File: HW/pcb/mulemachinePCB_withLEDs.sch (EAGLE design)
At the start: 29 parts, among them IC1 LD117AV50, IC2 MEGA8-P, J1 DCJ0202, Q1 16Mhz

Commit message: finished layout for PCB. implemented trace widths for PWR and GND. Lined up hole placement to match with Front panel laser design.
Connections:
- net N$7 renamed P1
- net N$8 renamed P2
- net N$9 renamed P3
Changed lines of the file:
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@@
 <clearance class="0" value="0.254"/>
 </class>
-<class number="1" name="Power" width="0.508" drill="0.508">
+<class number="1" name="Power" width="0.7874" drill="0.508">
 <clearance class="1" value="0.254"/>
 </class>
@@
 </segment>
 </net>
-<net name="N$7" class="0">
+<net name="P1" class="1">
 <segment>
 <pinref part="T1" gate="G$1" pin="C"/>
@@
 <pinref part="D1" gate="1" pin="A"/>
 <wire x1="165.1" y1="104.14" x2="157.48" y2="104.14" width="0.1524" layer="91"/>
-</segment>
-</net>
-<net name="N$8" class="0">
+<label x="147.32" y="99.06" size="1.778" layer="95"/>
+</segment>
+</net>
+<net name="P2" class="1">
 <segment>
 <pinref part="X2" gate="G$1" pin="5"/>
@@
 <pinref part="D2" gate="1" pin="A"/>
 <wire x1="165.1" y1="96.52" x2="157.48" y2="96.52" width="0.1524" layer="91"/>
-</segment>
-</net>
-<net name="N$9" class="0">
+<label x="162.56" y="91.44" size="1.778" layer="95"/>
+</segment>
+</net>
+<net name="P3" class="1">
 <segment>
 <pinref part="X2" gate="G$1" pin="9"/>
@@
 <wire x1="195.58" y1="86.36" x2="195.58" y2="93.98" width="0.1524" layer="91"/>
 <junction x="195.58" y="93.98"/>
-</segment>
-</net>
+<label x="203.2" y="91.44" size="1.778" layer="95"/>
+</segment>
+</net>

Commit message: ordered MM v1.0 of PCB. Gerber files contained in HW/pcb/mulemachinePCB_withLEDs_2022-02-17.zip
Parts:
- C5: value (none) -> 470uF
- R7: value 200 -> 10k
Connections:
- removed net SWTPOT: IC2.PC4(ADC4/SDA), R11.S
- new net SOURRPOT: IC2.PC5(ADC5/SCL), R10.S
- net STRPOT: now also IC2.PC4(ADC4/SDA), R11.S; no longer IC2.PC5(ADC5/SCL), R10.S
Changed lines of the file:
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@@
 <part name="C2" library="capacitor-wima" library_urn="urn:adsk.eagle:library:116" deviceset="C" device="2,5-3" package3d_urn="urn:adsk.eagle:package:5436/1" value="22pF"/>
 <part name="C3" library="capacitor-wima" library_urn="urn:adsk.eagle:library:116" deviceset="C" device="2,5-3" package3d_urn="urn:adsk.eagle:package:5436/1" value="22pF"/>
-<part name="R7" library="rcl" library_urn="urn:adsk.eagle:library:334" deviceset="R-US_" device="0207/10" package3d_urn="urn:adsk.eagle:package:23491/2" value="200"/>
+<part name="R7" library="rcl" library_urn="urn:adsk.eagle:library:334" deviceset="R-US_" device="0207/10" package3d_urn="urn:adsk.eagle:package:23491/2" value="10k"/>
 <part name="SUPPLY1" library="supply2" library_urn="urn:adsk.eagle:library:372" deviceset="GND" device=""/>
 <part name="LED1" library="led" library_urn="urn:adsk.eagle:library:259" deviceset="LED" device="5MM" package3d_urn="urn:adsk.eagle:package:15799/2"/>
@@
 <part name="R10" library="pot" library_urn="urn:adsk.eagle:library:331" deviceset="US-EVU" device="L" package3d_urn="urn:adsk.eagle:package:22736/1" technology="F3"/>
 <part name="R11" library="pot" library_urn="urn:adsk.eagle:library:331" deviceset="US-EVU" device="L" package3d_urn="urn:adsk.eagle:package:22736/1" technology="F3"/>
-<part name="C5" library="rcl" library_urn="urn:adsk.eagle:library:334" deviceset="CPOL-US" device="153CLV-0605" package3d_urn="urn:adsk.eagle:package:23398/2"/>
+<part name="C5" library="rcl" library_urn="urn:adsk.eagle:library:334" deviceset="CPOL-US" device="153CLV-0605" package3d_urn="urn:adsk.eagle:package:23398/2" value="470uF"/>
 <part name="SUPPLY11" library="supply2" library_urn="urn:adsk.eagle:library:372" deviceset="GND" device=""/>
 <part name="C1" library="capacitor-wima" library_urn="urn:adsk.eagle:library:116" deviceset="C" device="2,5-3" package3d_urn="urn:adsk.eagle:package:5436/1" value="0.1uF"/>
@@
 </segment>
 </net>
-<net name="SWTPOT" class="0">
+<net name="STRPOT" class="0">
 <segment>
 <wire x1="86.36" y1="22.86" x2="96.52" y2="22.86" width="0.1524" layer="91"/>
@@
 </segment>
 </net>
-<net name="STRPOT" class="0">
+<net name="SOURRPOT" class="0">
 <segment>
 <wire x1="86.36" y1="-12.7" x2="96.52" y2="-12.7" width="0.1524" layer="91"/>

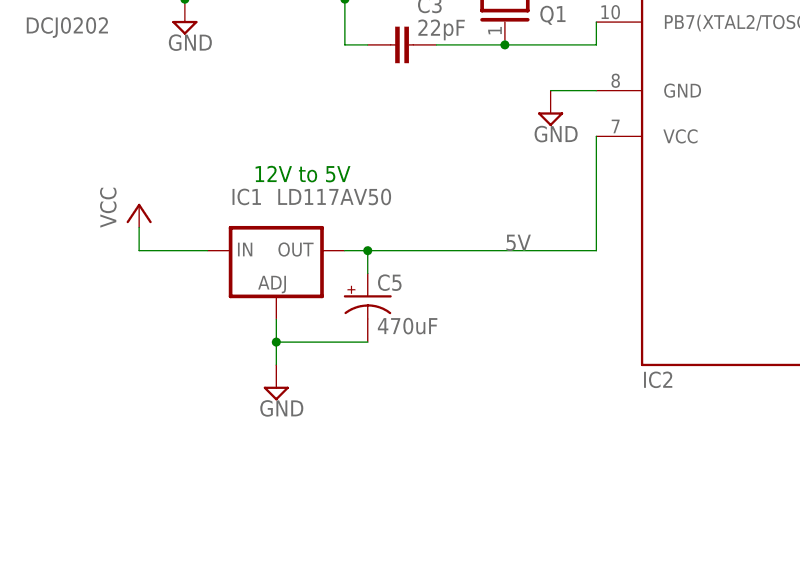
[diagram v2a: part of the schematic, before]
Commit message: fixed issue #7 on PCB. not yet ordered or tested on physical HW. schematic functionality should not change. just modified capacitor packaging
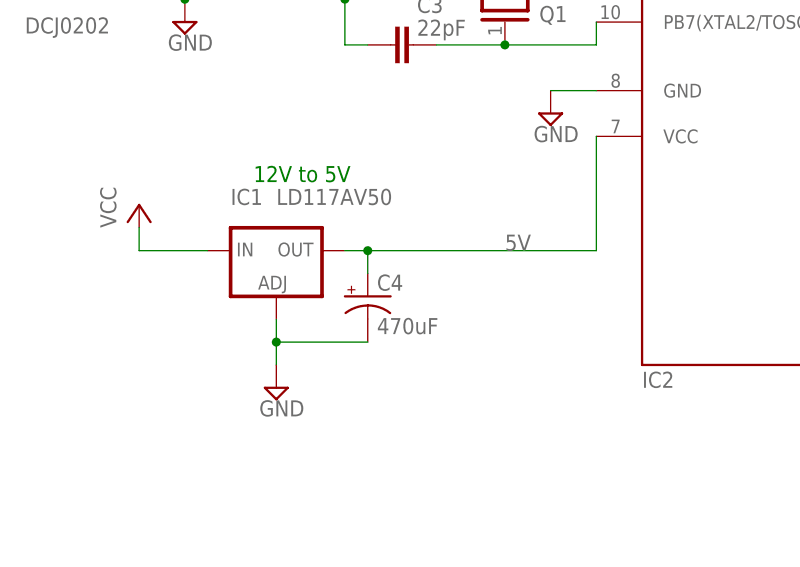
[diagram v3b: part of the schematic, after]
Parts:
- removed C5: 470uF, rcl:CPOL-US153CLV-0605
- added C4: 470uF, rcl:CPOL-USE2.5-6
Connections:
- net 5V: now also C4.+; no longer C5.+
- net GND: now also C4.-; no longer C5.-
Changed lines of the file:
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@@
 <part name="R10" library="pot" library_urn="urn:adsk.eagle:library:331" deviceset="US-EVU" device="L" package3d_urn="urn:adsk.eagle:package:22736/1" technology="F3"/>
 <part name="R11" library="pot" library_urn="urn:adsk.eagle:library:331" deviceset="US-EVU" device="L" package3d_urn="urn:adsk.eagle:package:22736/1" technology="F3"/>
-<part name="C5" library="rcl" library_urn="urn:adsk.eagle:library:334" deviceset="CPOL-US" device="153CLV-0605" package3d_urn="urn:adsk.eagle:package:23398/2" value="470uF"/>
 <part name="SUPPLY11" library="supply2" library_urn="urn:adsk.eagle:library:372" deviceset="GND" device=""/>
 <part name="C1" library="capacitor-wima" library_urn="urn:adsk.eagle:library:116" deviceset="C" device="2,5-3" package3d_urn="urn:adsk.eagle:package:5436/1" value="0.1uF"/>
+<part name="C4" library="rcl" library_urn="urn:adsk.eagle:library:334" deviceset="CPOL-US" device="E2.5-6" package3d_urn="urn:adsk.eagle:package:23349/1" value="470uF"/>
 </parts>
 <sheets>
@@
 <attribute name="NAME" x="104.14" y="22.86" size="1.778" layer="95"/>
 </instance>
-<instance part="C5" gate="G$1" x="0" y="30.48" smashed="yes">
-<attribute name="NAME" x="1.016" y="31.115" size="1.778" layer="95"/>
-<attribute name="VALUE" x="1.016" y="26.289" size="1.778" layer="96"/>
-</instance>
 <instance part="SUPPLY11" gate="GND" x="20.32" y="50.8" smashed="yes">
 <attribute name="VALUE" x="18.415" y="47.625" size="1.778" layer="96"/>
@@
 <attribute name="NAME" x="13.081" y="77.216" size="1.778" layer="95"/>
 <attribute name="VALUE" x="18.161" y="77.216" size="1.778" layer="96"/>
+</instance>
+<instance part="C4" gate="G$1" x="0" y="30.48" smashed="yes">
+<attribute name="NAME" x="1.016" y="31.115" size="1.778" layer="95"/>
+<attribute name="VALUE" x="1.016" y="26.289" size="1.778" layer="96"/>
 </instance>
 </instances>
@@
 <wire x1="0" y1="25.4" x2="-10.16" y2="25.4" width="0.1524" layer="91"/>
 <junction x="-10.16" y="25.4"/>
-<pinref part="C5" gate="G$1" pin="-"/>
+<pinref part="C4" gate="G$1" pin="-"/>
 </segment>
 <segment>
@@
 <wire x1="25.4" y1="35.56" x2="25.4" y2="48.26" width="0.1524" layer="91"/>
 <label x="15.24" y="35.56" size="1.778" layer="95"/>
-<pinref part="C5" gate="G$1" pin="+"/>
-</segment>
-<segment>
+<pinref part="C4" gate="G$1" pin="+"/>
+</segment>
+<segment>

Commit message: fixed issue #8 where the transistor pinout was backwards. fixed for next PCB order
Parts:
- T1, T2, T3: device transistor:MPS2222A-NPN-TO92-CBE -> transistor-neu-to92:2N4401-NPN-TO92-EBC

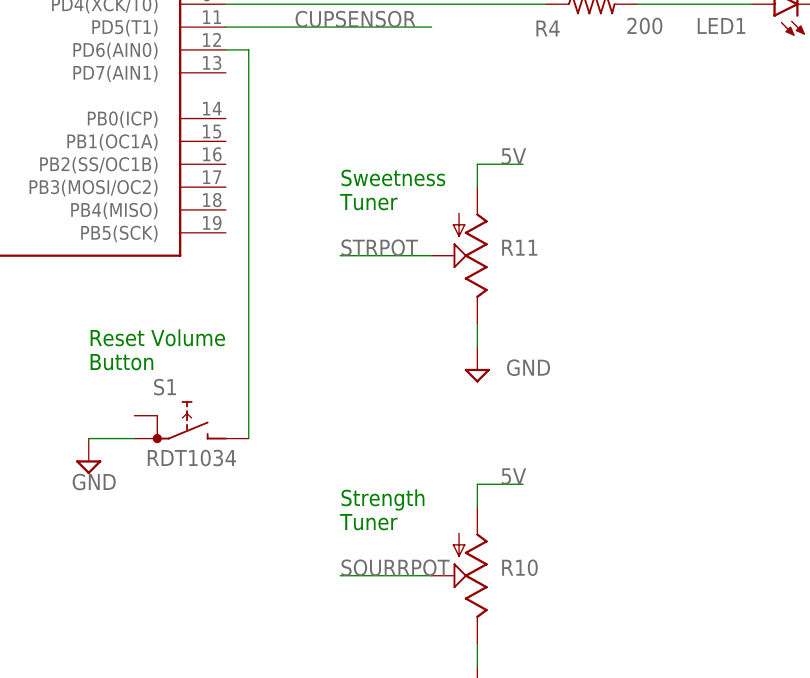
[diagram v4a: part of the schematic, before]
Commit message: changed resistor packaging to 0411/12 for new 100 and 200 ohm 2Watt resistors purchased.
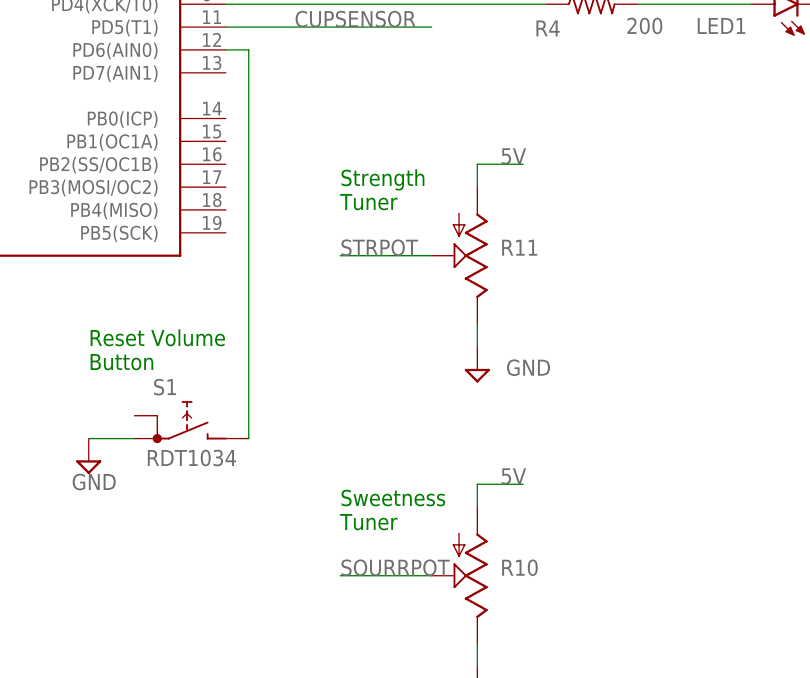
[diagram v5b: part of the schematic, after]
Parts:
- R1, R2, R3, R4, R5, R6: device rcl:R-US_0207/10 -> rcl:R-US_0411/12
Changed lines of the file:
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@@
 <grid distance="0.1" unitdist="inch" unit="inch" style="lines" multiple="1" display="no" altdistance="0.01" altunitdist="inch" altunit="inch"/>
 <layers>
-<layer number="1" name="Top" color="4" fill="1" visible="no" active="no"/>
-<layer number="16" name="Bottom" color="1" fill="1" visible="no" active="no"/>
-<layer number="17" name="Pads" color="2" fill="1" visible="no" active="no"/>
-<layer number="18" name="Vias" color="2" fill="1" visible="no" active="no"/>
-<layer number="19" name="Unrouted" color="6" fill="1" visible="no" active="no"/>
-<layer number="20" name="Dimension" color="15" fill="1" visible="no" active="no"/>
-<layer number="21" name="tPlace" color="7" fill="1" visible="no" active="no"/>
-<layer number="22" name="bPlace" color="7" fill="1" visible="no" active="no"/>
-<layer number="23" name="tOrigins" color="15" fill="1" visible="no" active="no"/>
-<layer number="24" name="bOrigins" color="15" fill="1" visible="no" active="no"/>
-<layer number="25" name="tNames" color="7" fill="1" visible="no" active="no"/>
-<layer number="26" name="bNames" color="7" fill="1" visible="no" active="no"/>
-<layer number="27" name="tValues" color="7" fill="1" visible="no" active="no"/>
-<layer number="28" name="bValues" color="7" fill="1" visible="no" active="no"/>
+<layer number="1" name="Top" color="4" fill="1" visible="yes" active="no"/>
+<layer number="16" name="Bottom" color="1" fill="1" visible="yes" active="no"/>
+<layer number="17" name="Pads" color="2" fill="1" visible="yes" active="no"/>
+<layer number="18" name="Vias" color="2" fill="1" visible="yes" active="no"/>
+<layer number="19" name="Unrouted" color="6" fill="1" visible="yes" active="no"/>
+<layer number="20" name="Dimension" color="24" fill="1" visible="yes" active="no"/>
+<layer number="21" name="tPlace" color="7" fill="1" visible="yes" active="no"/>
+<layer number="22" name="bPlace" color="7" fill="1" visible="yes" active="no"/>
+<layer number="23" name="tOrigins" color="15" fill="1" visible="yes" active="no"/>
+<layer number="24" name="bOrigins" color="15" fill="1" visible="yes" active="no"/>
+<layer number="25" name="tNames" color="7" fill="1" visible="yes" active="no"/>
+<layer number="26" name="bNames" color="7" fill="1" visible="yes" active="no"/>
+<layer number="27" name="tValues" color="7" fill="1" visible="yes" active="no"/>
+<layer number="28" name="bValues" color="7" fill="1" visible="yes" active="no"/>
 <layer number="29" name="tStop" color="7" fill="3" visible="no" active="no"/>
 <layer number="30" name="bStop" color="7" fill="6" visible="no" active="no"/>
@@
 <layer number="35" name="tGlue" color="7" fill="4" visible="no" active="no"/>
 <layer number="36" name="bGlue" color="7" fill="5" visible="no" active="no"/>
-<layer number="37" name="tTest" color="7" fill="1" visible="no" active="no"/>
-<layer number="38" name="bTest" color="7" fill="1" visible="no" active="no"/>
+<layer number="37" name="tTest" color="7" fill="1" visible="yes" active="no"/>
+<layer number="38" name="bTest" color="7" fill="1" visible="yes" active="no"/>
 <layer number="39" name="tKeepout" color="4" fill="11" visible="no" active="no"/>
 <layer number="40" name="bKeepout" color="1" fill="11" visible="no" active="no"/>
@@
 <layer number="44" name="Drills" color="7" fill="1" visible="no" active="no"/>
 <layer number="45" name="Holes" color="7" fill="1" visible="no" active="no"/>
-<layer number="46" name="Milling" color="3" fill="1" visible="no" active="no"/>
-<layer number="47" name="Measures" color="7" fill="1" visible="no" active="no"/>
-<layer number="48" name="Document" color="7" fill="1" visible="no" active="no"/>
-<layer number="49" name="Reference" color="7" fill="1" visible="no" active="no"/>
-<layer number="51" name="tDocu" color="7" fill="1" visible="no" active="no"/>
-<layer number="52" name="bDocu" color="7" fill="1" visible="no" active="no"/>
+<layer number="46" name="Milling" color="3" fill="1" visible="yes" active="no"/>
+<layer number="47" name="Measures" color="7" fill="1" visible="yes" active="no"/>
+<layer number="48" name="Document" color="7" fill="1" visible="yes" active="no"/>
+<layer number="49" name="Reference" color="7" fill="1" visible="yes" active="no"/>
+<layer number="51" name="tDocu" color="7" fill="1" visible="yes" active="no"/>
+<layer number="52" name="bDocu" color="7" fill="1" visible="yes" active="no"/>
 <layer number="88" name="SimResults" color="9" fill="1" visible="yes" active="yes"/>
 <layer number="89" name="SimProbes" color="9" fill="1" visible="yes" active="yes"/>
@@
 <part name="D2" library="diode" library_urn="urn:adsk.eagle:library:210" deviceset="1N4004" device="" package3d_urn="urn:adsk.eagle:package:43336/1"/>
 <part name="D3" library="diode" library_urn="urn:adsk.eagle:library:210" deviceset="1N4004" device="" package3d_urn="urn:adsk.eagle:package:43336/1"/>
-<part name="R1" library="rcl" library_urn="urn:adsk.eagle:library:334" deviceset="R-US_" device="0207/10" package3d_urn="urn:adsk.eagle:package:23491/2" value="150"/>
-<part name="R2" library="rcl" library_urn="urn:adsk.eagle:library:334" deviceset="R-US_" device="0207/10" package3d_urn="urn:adsk.eagle:package:23491/2" value="150"/>
-<part name="R3" library="rcl" library_urn="urn:adsk.eagle:library:334" deviceset="R-US_" device="0207/10" package3d_urn="urn:adsk.eagle:package:23491/2" value="150"/>
-<part name="R4" library="rcl" library_urn="urn:adsk.eagle:library:334" deviceset="R-US_" device="0207/10" package3d_urn="urn:adsk.eagle:package:23491/2" value="200"/>
-<part name="R5" library="rcl" library_urn="urn:adsk.eagle:library:334" deviceset="R-US_" device="0207/10" package3d_urn="urn:adsk.eagle:package:23491/2" value="200"/>
-<part name="R6" library="rcl" library_urn="urn:adsk.eagle:library:334" deviceset="R-US_" device="0207/10" package3d_urn="urn:adsk.eagle:package:23491/2" value="200"/>
+<part name="R1" library="rcl" library_urn="urn:adsk.eagle:library:334" deviceset="R-US_" device="0411/12" package3d_urn="urn:adsk.eagle:package:23578/1" value="150"/>
+<part name="R2" library="rcl" library_urn="urn:adsk.eagle:library:334" deviceset="R-US_" device="0411/12" package3d_urn="urn:adsk.eagle:package:23578/1" value="150"/>
+<part name="R3" library="rcl" library_urn="urn:adsk.eagle:library:334" deviceset="R-US_" device="0411/12" package3d_urn="urn:adsk.eagle:package:23578/1" value="150"/>
+<part name="R4" library="rcl" library_urn="urn:adsk.eagle:library:334" deviceset="R-US_" device="0411/12" package3d_urn="urn:adsk.eagle:package:23578/1" value="200"/>
+<part name="R5" library="rcl" library_urn="urn:adsk.eagle:library:334" deviceset="R-US_" device="0411/12" package3d_urn="urn:adsk.eagle:package:23578/1" value="200"/>
+<part name="R6" library="rcl" library_urn="urn:adsk.eagle:library:334" deviceset="R-US_" device="0411/12" package3d_urn="urn:adsk.eagle:package:23578/1" value="200"/>
 <part name="S1" library="switch" library_urn="urn:adsk.eagle:library:380" deviceset="RDT1034" device="" package3d_urn="urn:adsk.eagle:package:27704/1"/>
 <part name="IC1" library="v-reg" library_urn="urn:adsk.eagle:library:409" deviceset="LD117A?*" device="V" package3d_urn="urn:adsk.eagle:package:30365/1" technology="50"/>
@@
 <text x="124.46" y="60.96" size="1.778" layer="91">USER INTERFACE</text>
 <text x="182.88" y="111.76" size="1.778" layer="91">Harness</text>
-<text x="86.36" y="27.94" size="1.778" layer="91">Sweetness
+<text x="86.36" y="-7.62" size="1.778" layer="91">Sweetness
 Tuner</text>
-<text x="86.36" y="-7.62" size="1.778" layer="91">Strength
+<text x="86.36" y="27.94" size="1.778" layer="91">Strength
 Tuner</text>
 <text x="132.08" y="104.14" size="1.778" layer="91">0.15A each motor</text>
